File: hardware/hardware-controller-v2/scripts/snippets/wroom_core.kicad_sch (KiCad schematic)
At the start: 7 parts, among them U2 ESP32-WROOM-32E

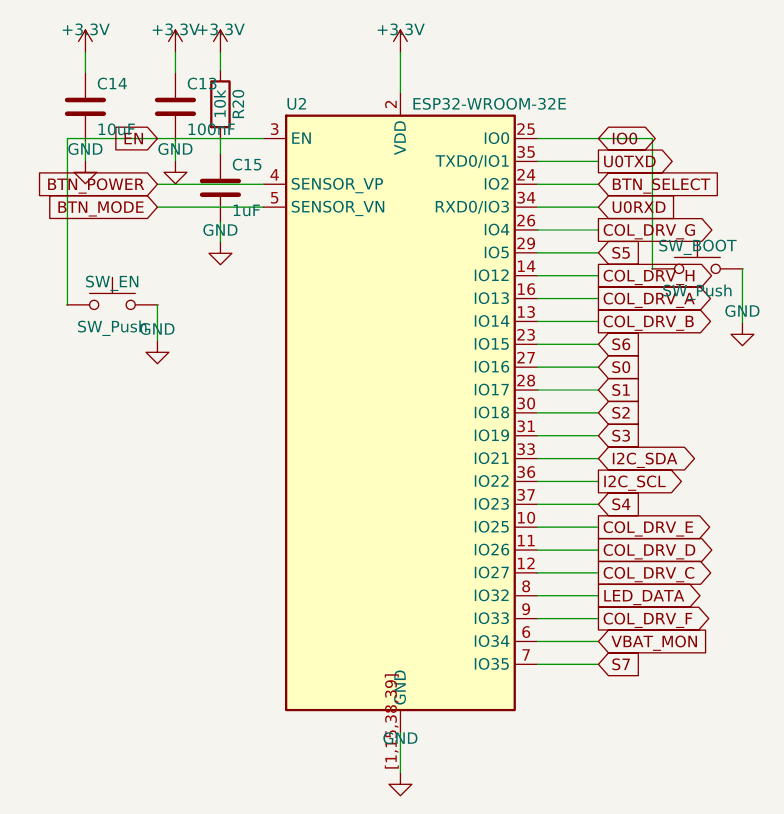
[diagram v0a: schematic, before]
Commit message: fix(hw): connect floating SW_EN/SW_BOOT pins in WROOM core snippet
SW_Push pins sit at +/-5.08mm from symbol origin; switches placed at
integer x put pins 0.08mm off the wire endpoints, leaving both boot-
critical buttons electrically floating (zero net memberships).

Moved SW_EN to (68.08,88) and SW_BOOT to (133.08,84) so pin 1 lands
exactly on the existing wire; shifted each pin-2 GND stub and power
symbol to the true pin-2 x (73.16 / 138.16). Verified: netlist now has
SW_EN in {EN,GND}, SW_BOOT in {IO0,GND}; systematic pin-vs-wire sweep
of all 59 pins across every symbol passes; ERC violations 100 -> 91.

Co-Authored-By: Claude Fable 5 <noreply@anthropic.com>
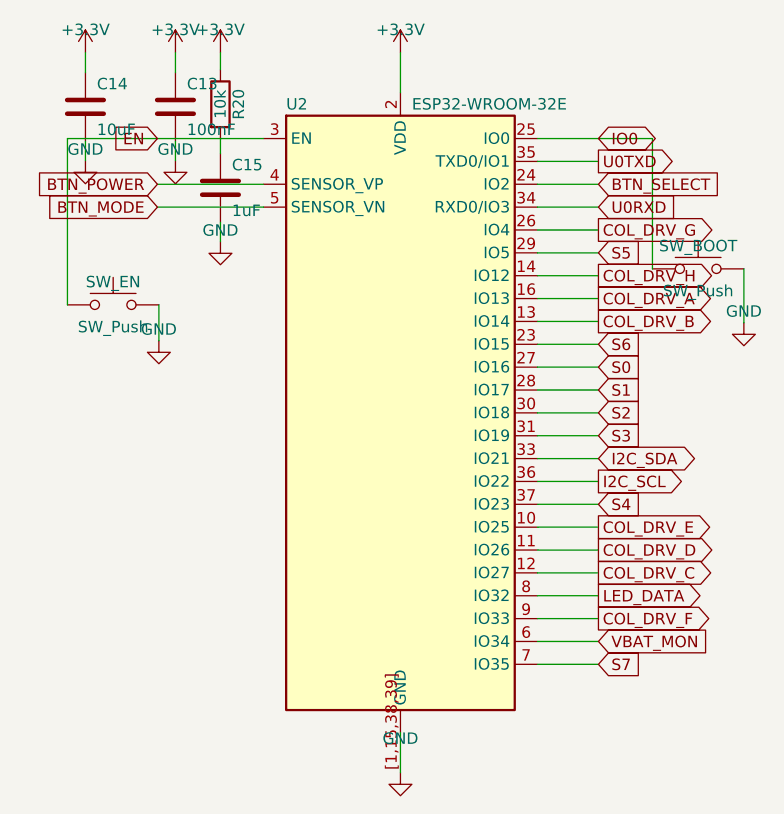
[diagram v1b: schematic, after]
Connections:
- net EN: now also SW_EN.1
- net GND: now also SW_BOOT.2, SW_EN.2
- net IO0: now also SW_BOOT.1
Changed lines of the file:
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@@
 	(symbol
 		(lib_id "Switch:SW_Push")
-		(at 68 88 0)
+		(at 68.08 88 0)
 		(unit 1)
 		(exclude_from_sim no)
@@
 		(uuid "wr320009-0000-4000-8000-000000000001")
 		(property "Reference" "SW_EN"
-			(at 68 85.46 0)
+			(at 68.08 85.46 0)
 			(effects (font (size 1.27 1.27)))
 		)
 		(property "Value" "SW_Push"
-			(at 68 90.46 0)
+			(at 68.08 90.46 0)
 			(effects (font (size 1.27 1.27)))
 		)
 		(property "Footprint" "Button_Switch_SMD:SW_SPST_SKQG_WithoutStem"
-			(at 68 88 0)
+			(at 68.08 88 0)
 			(effects (font (size 1.27 1.27)) (hide yes))
 		)
 		(property "Datasheet" ""
-			(at 68 88 0)
+			(at 68.08 88 0)
 			(effects (font (size 1.27 1.27)) (hide yes))
 		)
 		(property "Description" ""
-			(at 68 88 0)
+			(at 68.08 88 0)
 			(effects (font (size 1.27 1.27)) (hide yes))
 		)
@@
 	)
 	(wire
-		(pts (xy 73 88) (xy 73 92))
+		(pts (xy 73.16 88) (xy 73.16 92))
 		(stroke (width 0) (type default))
 		(uuid "wr320009-0000-4000-8000-000000000006")
@@
 	(symbol
 		(lib_id "power:GND")
-		(at 73 92 0)
+		(at 73.16 92 0)
 		(unit 1)
 		(exclude_from_sim no)
@@
 		(uuid "wr320009-0000-4000-8000-000000000007")
 		(property "Reference" "#PWR?"
-			(at 73 94 0)
+			(at 73.16 94 0)
 			(effects (font (size 1.27 1.27)) (hide yes))
 		)
 		(property "Value" "GND"
-			(at 73 90.73 0)
+			(at 73.16 90.73 0)
 			(effects (font (size 1.27 1.27)))
 		)
 		(property "Footprint" ""
-			(at 73 92 0)
+			(at 73.16 92 0)
 			(effects (font (size 1.27 1.27)) (hide yes))
 		)
@@
 	(symbol
 		(lib_id "Switch:SW_Push")
-		(at 133 84 0)
+		(at 133.08 84 0)
 		(unit 1)
 		(exclude_from_sim no)
@@
 		(uuid "wr32000c-0000-4000-8000-000000000005")
 		(property "Reference" "SW_BOOT"
-			(at 133 81.46 0)
+			(at 133.08 81.46 0)
 			(effects (font (size 1.27 1.27)))
 		)
 		(property "Value" "SW_Push"
-			(at 133 86.46 0)
+			(at 133.08 86.46 0)
 			(effects (font (size 1.27 1.27)))
 		)
 		(property "Footprint" "Button_Switch_SMD:SW_SPST_SKQG_WithoutStem"
-			(at 133 84 0)
+			(at 133.08 84 0)
 			(effects (font (size 1.27 1.27)) (hide yes))
 		)
 		(property "Datasheet" ""
-			(at 133 84 0)
+			(at 133.08 84 0)
 			(effects (font (size 1.27 1.27)) (hide yes))
 		)
 		(property "Description" ""
-			(at 133 84 0)
+			(at 133.08 84 0)
 			(effects (font (size 1.27 1.27)) (hide yes))
 		)
@@
 	)
 	(wire
-		(pts (xy 138 84) (xy 138 90))
+		(pts (xy 138.16 84) (xy 138.16 90))
 		(stroke (width 0) (type default))
 		(uuid "wr32000c-0000-4000-8000-000000000008")
@@
 	(symbol
 		(lib_id "power:GND")
-		(at 138 90 0)
+		(at 138.16 90 0)
 		(unit 1)
 		(exclude_from_sim no)
@@
 		(uuid "wr32000c-0000-4000-8000-000000000009")
 		(property "Reference" "#PWR?"
-			(at 138 92 0)
+			(at 138.16 92 0)
 			(effects (font (size 1.27 1.27)) (hide yes))
 		)
 		(property "Value" "GND"
-			(at 138 88.73 0)
+			(at 138.16 88.73 0)
 			(effects (font (size 1.27 1.27)))
 		)
 		(property "Footprint" ""
-			(at 138 90 0)
-			(effects (font (size 1.27 1.27)) (hide yes))
-		)
+			(at 138.16 90 0)
+			(effects (font (size 1.27 1.27)) (hide yes))
+		)
